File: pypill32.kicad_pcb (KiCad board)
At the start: 2 copper layers, 52.1 x 27.9 mm, 45 parts, among them J1 HeaderR, J2 HeaderL, J3 USB_PINS, J4 SWD_HEADER, SW1 RST_BTN, SW2 BOOT_BTN, U1 SRV05-4, U2 PY32F030F18P6, U3 CH340N, U4 AMS1117-3.3, Y1 32.768 kHz

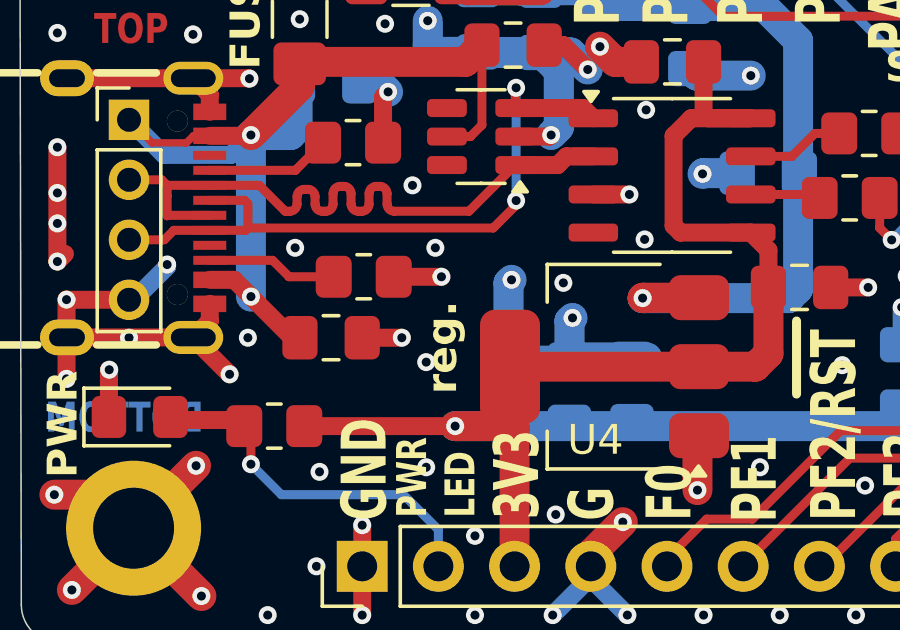
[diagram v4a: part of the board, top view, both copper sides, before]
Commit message: added pad for RTS pin
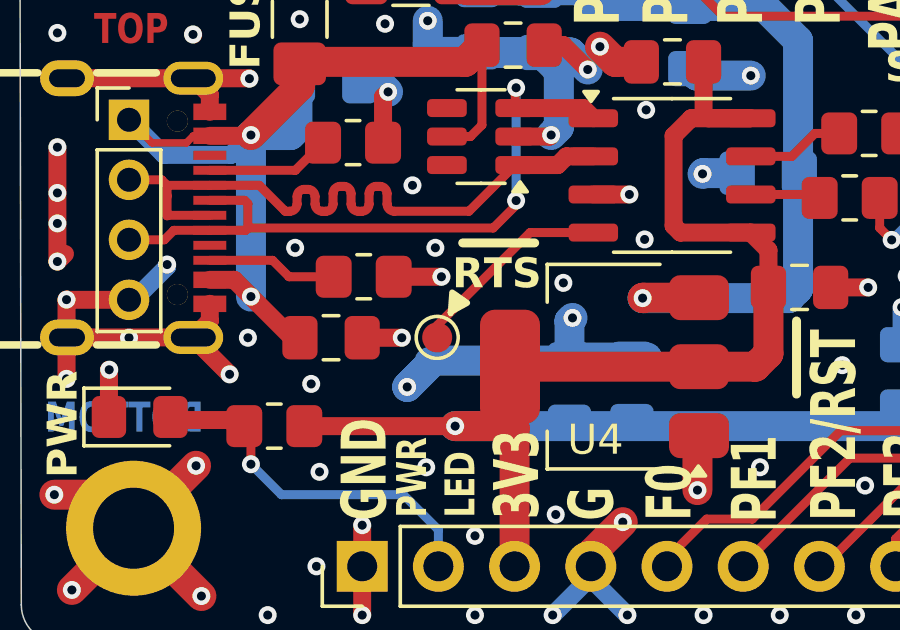
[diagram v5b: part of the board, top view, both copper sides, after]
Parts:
- added TP2: RTS_pad, TestPoint:TestPoint_Pad_D1.0mm, F.Cu at (104.1, 80.0)
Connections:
- U3 pad 4: unconnected-(U3-~{RTS}-Pad4) -> Net-(U3-~{RTS})
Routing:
- net Net-(U3-~{RTS}): track 0.00 -> 6.89 mm
- net GND: track 108.4 -> 110.6 mm
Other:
- board text added: "RTS"
- board text removed: "reg."
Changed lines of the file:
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@@
 	(net 2 "Net-(U3-RXD)")
 	(net 3 "GND")
-	(net 4 "unconnected-(U3-~{RTS}-Pad4)")
+	(net 4 "Net-(U3-~{RTS})")
 	(net 5 "+5V")
 	(net 6 "Net-(U3-TXD)")
@@
 			(layers "F.Cu" "F.Paste" "F.Mask")
 			(roundrect_rratio 0.25)
-			(net 4 "unconnected-(U3-~{RTS}-Pad4)")
+			(net 4 "Net-(U3-~{RTS})")
 			(pinfunction "~{RTS}")
 			(pintype "output")
@@
 		)
 	)
+	(footprint "TestPoint:TestPoint_Pad_D1.0mm"
+		(layer "F.Cu")
+		(at 104.1 80)
+		(descr "SMD pad as test Point, diameter 1.0mm")
+		(tags "test point SMD pad")
+		(property "Reference" "TP2"
+			(at 0 -1.448 0)
+			(layer "F.SilkS")
+			(hide yes)
+			(effects
+				(font
+					(size 1 1)
+					(thickness 0.15)
+				)
+			)
+		)
+		(property "Value" "RTS_pad"
+			(at 0 1.55 0)
+			(layer "F.Fab")
+			(effects
+				(font
+					(size 1 1)
+					(thickness 0.15)
+				)
+			)
+		)
+		(property "Footprint" "TestPoint:TestPoint_Pad_D1.0mm"
+			(at 0 0 0)
+			(unlocked yes)
+			(layer "F.Fab")
+			(hide yes)
+			(effects
+				(font
+					(size 1.27 1.27)
+					(thickness 0.15)
+				)
+			)
+		)
+		(property "Datasheet" ""
+			(at 0 0 0)
+			(unlocked yes)
+			(layer "F.Fab")
+			(hide yes)
+			(effects
+				(font
+					(size 1.27 1.27)
+					(thickness 0.15)
+				)
+			)
+		)
+		(property "Description" "test point"
+			(at 0 0 0)
+			(unlocked yes)
+			(layer "F.Fab")
+			(hide yes)
+			(effects
+				(font
+					(size 1.27 1.27)
+					(thickness 0.15)
+				)
+			)
+		)
+		(property ki_fp_filters "Pin* Test*")
+		(sheetname "Root")
+		(sheetfile "pypill32.kicad_sch")
+		(attr exclude_from_pos_files)
+		(fp_circle
+			(center 0 0)
+			(end 0 0.7)
+			(stroke
+				(width 0.12)
+				(type solid)
+			)
+			(fill none)
+			(layer "F.SilkS")
+		)
+		(fp_circle
+			(center 0 0)
+			(end 1 0)
+			(stroke
+				(width 0.05)
+				(type solid)
+			)
+			(fill none)
+			(layer "F.CrtYd")
+		)
+		(fp_text user "${REFERENCE}"
+			(at 0 -1.45 0)
+			(layer "F.Fab")
+			(effects
+				(font
+					(size 1 1)
+					(thickness 0.15)
+				)
+			)
+		)
+		(pad "1" smd circle
+			(at 0 0)
+			(size 1 1)
+			(layers "F.Cu" "F.Mask")
+			(net 4 "Net-(U3-~{RTS})")
+			(pinfunction "1")
+			(pintype "passive")
+		)
+	)
 	(footprint "Connector_PinHeader_2.54mm:PinHeader_1x12_P2.54mm_Vertical"
 		(layer "F.Cu")
@@
 		(tags "resistor handsolder")
 		(property "Reference" "R6"
-			(at 2.5654 -0.0762 360)
+			(at 2.5654 -0.0762 0)
 			(layer "F.SilkS")
 			(hide yes)
@@
 		)
 		(property "Value" "0R"
-			(at 0 1.65 360)
+			(at 0 1.65 0)
 			(layer "F.Fab")
 			(effects
@@
 		)
 		(property "Footprint" "Resistor_SMD:R_0805_2012Metric_Pad1.20x1.40mm_HandSolder"
-			(at 0 0 360)
+			(at 0 0 0)
 			(layer "F.Fab")
 			(hide yes)
@@
 		)
 		(property "Datasheet" ""
-			(at 0 0 360)
+			(at 0 0 0)
 			(layer "F.Fab")
 			(hide yes)
@@
 		)
 		(property "Description" ""
-			(at 0 0 360)
+			(at 0 0 0)
 			(layer "F.Fab")
 			(hide yes)
@@
 		)
 		(fp_text user "${REFERENCE}"
-			(at 0 0 360)
+			(at 0 0 0)
 			(layer "F.Fab")
 			(effects
@@
 	)
 	(gr_line
+		(start 104.95 76.85)
+		(end 107.35 76.85)
+		(stroke
+			(width 0.3)
+			(type default)
+		)
+		(layer "F.SilkS")
+	)
+	(gr_poly
+		(pts
+			(xy 104.55 79.2) (xy 104.6 78.5) (xy 105.1 78.85) (xy 104.55 79.15)
+		)
+		(stroke
+			(width 0.2)
+			(type solid)
+		)
+		(fill solid)
+		(layer "F.SilkS")
+	)
+	(gr_line
 		(start 135.128 72.136)
 		(end 137.5664 72.136)
@@
 		)
 	)
+	(gr_text "RTS"
+		(at 104.6 78.45 0)
+		(layer "F.SilkS")
+		(effects
+			(font
+				(size 1 1)
+				(thickness 0.25)
+				(bold yes)
+			)
+			(justify left bottom)
+		)
+	)
 	(gr_text "PA2"
 		(at 123.0376 86.0552 90)
@@
 		)
 	)
-	(gr_text "reg."
-		(at 104.8512 81.8896 90)
-		(layer "F.SilkS")
-		(effects
-			(font
-				(size 1 1)
-				(thickness 0.25)
-				(bold yes)
-			)
-			(justify left bottom)
-		)
-	)
 	(gr_text "1"
 		(at 121.158 80.8228 0)
@@
 	)
 	(via
-		(at 103.7336 80.8228)
+		(at 103.1 81.65)
 		(size 0.6)
 		(drill 0.3)
@@
 	)
 	(via
+		(at 99.9 81.55)
+		(size 0.6)
+		(drill 0.3)
+		(layers "F.Cu" "B.Cu")
+		(free yes)
+		(net 3)
+	)
+	(via
 		(at 140.0556 83.6676)
 		(size 0.6)
@@
 	)
 	(via
-		(at 106.5784 78.0796)
-		(size 0.6)
-		(drill 0.3)
-		(layers "F.Cu" "B.Cu")
-		(free yes)
-		(net 3)
-	)
-	(via
 		(at 118.11 63.1952)
 		(size 0.6)
@@
 	(segment
 		(start 106.4768 80.772)
-		(end 106.4768 78.1812)
-		(width 1)
-		(layer "B.Cu")
-		(net 3)
-	)
-	(segment
-		(start 106.4768 80.772)
 		(end 108.4873 80.772)
 		(width 1)
@@
 	)
 	(segment
+		(start 103.978 80.772)
+		(end 106.4768 80.772)
+		(width 1)
+		(layer "B.Cu")
+		(net 3)
+	)
+	(segment
 		(start 105.4608 70.4811)
 		(end 104.0091 70.4811)
@@
 	)
 	(segment
+		(start 103.8352 80.9148)
+		(end 103.8352 80.8228)
+		(width 1)
+		(layer "B.Cu")
+		(net 3)
+	)
+	(segment
 		(start 111.0996 80.6704)
 		(end 108.5889 80.6704)
@@
 	)
 	(segment
-		(start 112.7545 71.2724)
-		(end 112.522 71.0399)
+		(start 103.1 81.65)
+		(end 103.978 80.772)
 		(width 1)
 		(layer "B.Cu")
@@
 	)
 	(segment
-		(start 106.4768 78.1812)
-		(end 106.5784 78.0796)
+		(start 112.7545 71.2724)
+		(end 112.522 71.0399)
 		(width 1)
 		(layer "B.Cu")
@@
 	)
 	(segment
+		(start 103.1 81.65)
+		(end 103.8352 80.9148)
+		(width 1)
+		(layer "B.Cu")
+		(net 3)
+	)
+	(segment
 		(start 109.22 87.63)
 		(end 109.22 87.9856)
@@
 	)
 	(segment
+		(start 104.1 79.6)
+		(end 107.1952 76.5048)
+		(width 0.3)
+		(layer "F.Cu")
+		(net 4)
+	)
+	(segment
+		(start 107.1952 76.5048)
+		(end 109.304 76.5048)
+		(width 0.3)
+		(layer "F.Cu")
+		(net 4)
+	)
+	(segment
+		(start 104.1 80)
+		(end 104.1 79.6)
+		(width 0.3)
+		(layer "F.Cu")
+		(net 4)
+	)
+	(segment

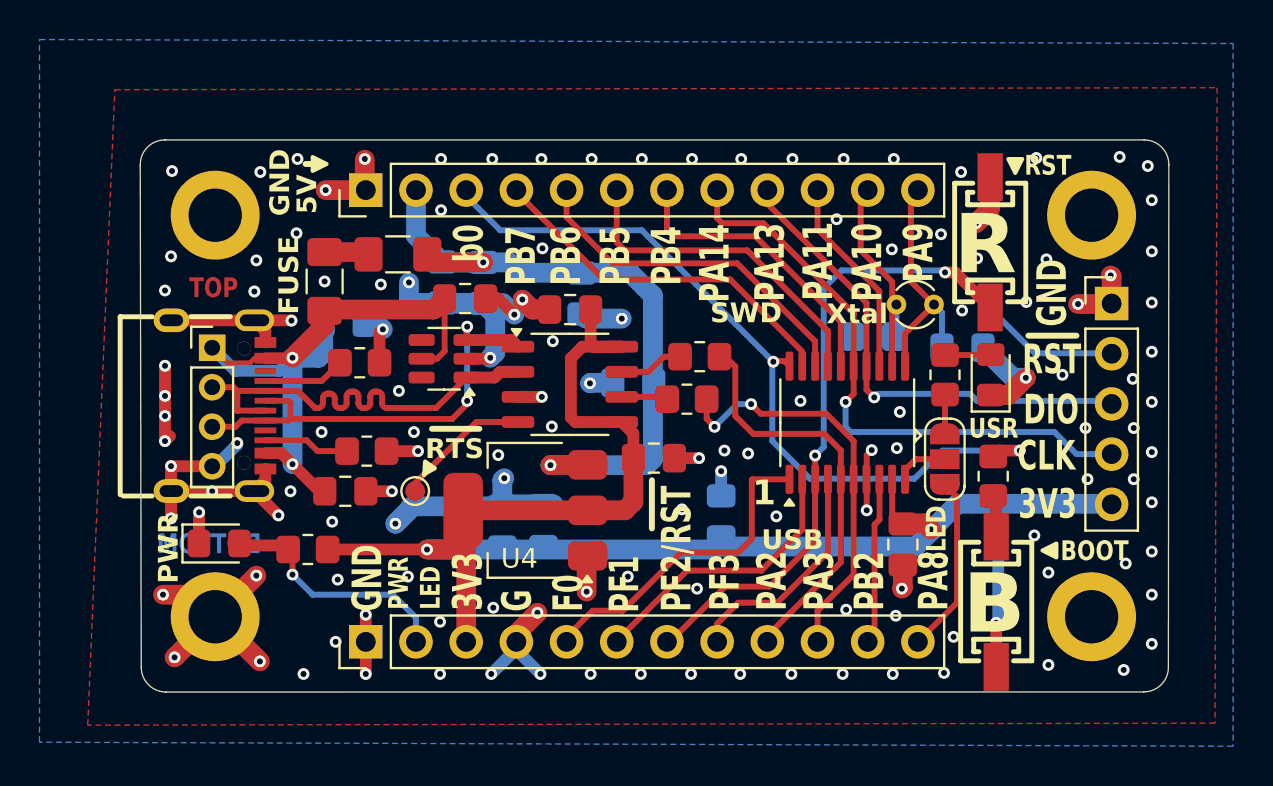
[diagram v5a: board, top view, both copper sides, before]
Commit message: added HF crystal
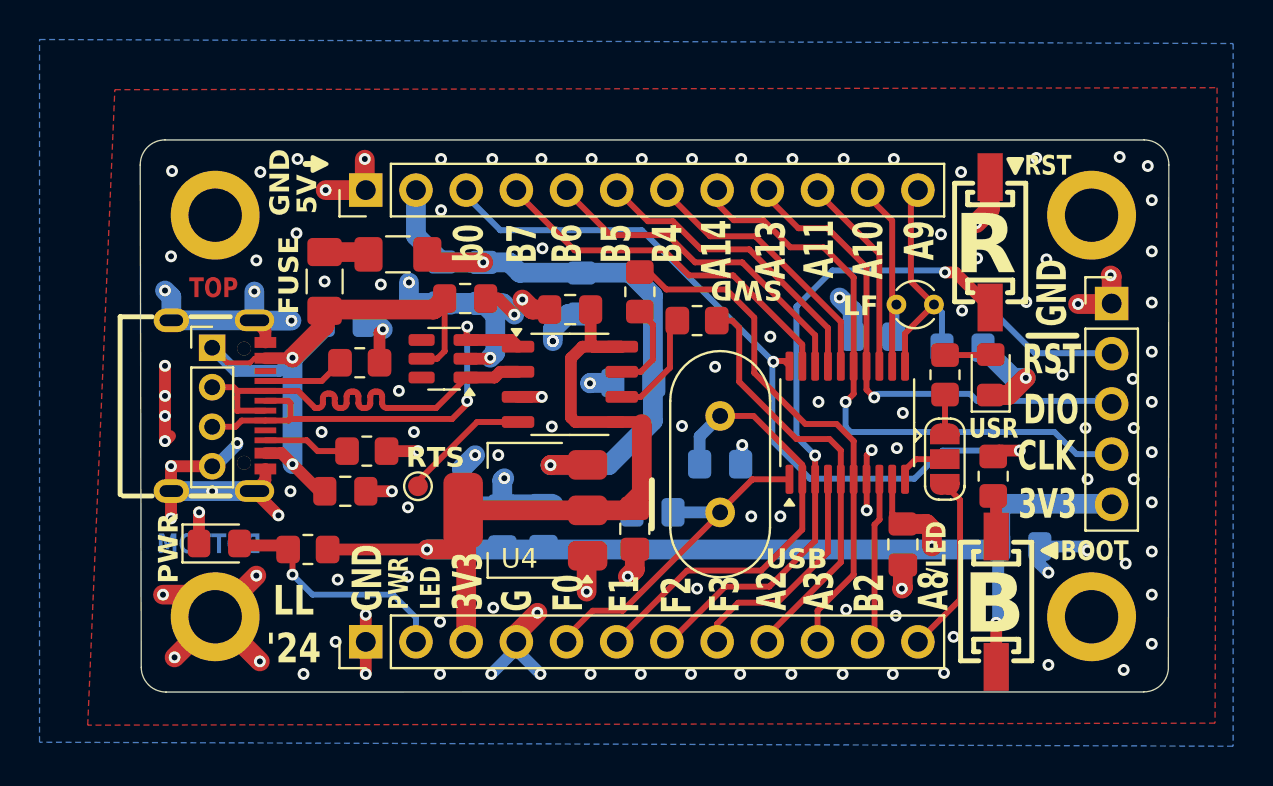
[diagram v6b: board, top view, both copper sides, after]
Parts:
- removed TP2: RTS_pad, TestPoint:TestPoint_Pad_D1.0mm
- added C17: 12p, Capacitor_SMD:C_0805_2012Metric_Pad1.18x1.45mm_HandSolder, B.Cu at (116.1, 81.1)
- added C18: 12p, Capacitor_SMD:C_0805_2012Metric_Pad1.18x1.45mm_HandSolder, B.Cu at (119.5, 78.6)
- added TP1: RTSn, TestPoint:TestPoint_Pad_D1.0mm, F.Cu at (104.2, 79.8)
- added Y2: 12M, Crystal:Crystal_HC49-4H_Vertical, F.Cu at (119.5, 76.2)
- moved C12 15.2 mm to (134.7, 82.8), turned to 0 degrees
- moved R5 4.47 mm to (115.5, 69.9), turned to 90 degrees
- moved R6 4.01 mm to (118.4, 71.4)
- moved C11 3.71 mm to (115.2, 81.9), turned to 90 degrees
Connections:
- R5 pad 2: PYUTX -> PYURX
- R6 pad 2: PYURX -> PYUTX
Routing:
- net GND: track 110.6 -> 122.7 mm, vias 133 -> 132
- net /PF1: track 14.3 -> 23.1 mm
- net PYURX: track 20.8 -> 26.9 mm, vias 2 -> 0
- net +3V3: track 89.0 -> 85.0 mm
- net Net-(U3-TXD): track 2.34 -> 5.59 mm
- net /PB5: track 17.0 -> 15.5 mm
- net Net-(U3-RXD): track 3.26 -> 4.54 mm
- net +5V: track 34.8 -> 33.7 mm
- net /PB4: track 15.0 -> 13.9 mm
- net NRST: track 42.4 -> 43.4 mm
- net SWDIO: track 25.0 -> 25.9 mm
- net VBUS: track 35.9 -> 35.1 mm
- net /PF0: track 16.6 -> 17.3 mm
- net SWDCLK: track 30.3 -> 30.9 mm
- net /PB6: track 17.8 -> 17.2 mm
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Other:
- board text added: "A10"
- board text added: "A11"
- board text added: "A13"
- board text added: "A13=SWDIO"
- board text added: "A14"
- board text added: "A14=SWCLK"
- board text added: "A2"
- board text added: "A3"
- board text added: "A8"
- board text added: "A9"
- board text added: "B2"
- board text added: "B4"
- board text added: "B5"
- board text added: "B6"
- board text added: "B7"
- board text added: "F1"
- board text added: "F2"
- board text added: "F3"
- board text added: "LF"
- board text added: "MCU: PY32F030 F18P6"
- board text removed: "1"
- board text removed: "8kB/64kB"
- board text removed: "PA10"
- board text removed: "PA11"
- board text removed: "PA13"
- board text removed: "PA13=SWDIO"
- board text removed: "PA14"
- board text removed: "PA14=SWCLK"
- board text removed: "PA2"
- board text removed: "PA3"
- board text removed: "PA8"
- board text removed: "PA9"
- board text removed: "PB2"
- board text removed: "PB4"
- board text removed: "PB5"
- board text removed: "PB6"
- board text removed: "PB7"
- board text removed: "PF0"
- board text removed: "PF1"
- board text removed: "PF2/RST"
- board text removed: "PF3"
- board text removed: "PY32F030F18P6"
- board text removed: "RST/PF2"
- board text removed: "Xtal"

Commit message: texts edit
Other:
- board text added: "XTAL"
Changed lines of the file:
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@@
+		)
+	)
+	(gr_text "XTAL"
+		(at 130.2512 69.9516 0)
+		(layer "B.SilkS")
+		(effects
+			(font
+				(size 1 1)
+				(thickness 0.25)
+				(bold yes)
+			)
+			(justify left bottom mirror)
 		)
 	)
@@
 		)
 	)
+	(gr_text "XTAL"
+		(at 114.3 84.4804 0)
+		(layer "B.SilkS")
+		(effects
+			(font
+				(size 1 1)
+				(thickness 0.25)
+				(bold yes)
+			)
+			(justify left bottom mirror)
+		)
+	)
 	(gr_text "B4"
 		(at 117.7544 65.7352 90)
@@
 	(gr_text "A11"
 		(at 125.4252 69.2404 90)
-		(layer "F.SilkS")
+		(layer "F.SilkS" knockout)
 		(effects
 			(font
@@
 	(gr_text "B7"
 		(at 110.3884 68.4784 90)
-		(layer "F.SilkS")
+		(layer "F.SilkS" knockout)
 		(effects
 			(font
@@
 	(gr_text "B5"
 		(at 115.1636 68.4784 90)
-		(layer "F.SilkS")
+		(layer "F.SilkS" knockout)
 		(effects
 			(font
@@
 	(gr_text "B6"
 		(at 112.6744 68.4784 90)
-		(layer "F.SilkS")
+		(layer "F.SilkS" knockout)
 		(effects
 			(font
@@
 	(gr_text "F3"
 		(at 120.65 86.1568 90)
-		(layer "F.SilkS")
+		(layer "F.SilkS" knockout)
 		(effects
 			(font
@@
 	(gr_text "B2"
 		(at 127.9652 86.1568 90)
-		(layer "F.SilkS")
+		(layer "F.SilkS" knockout)
 		(effects
 			(font
@@
 	(gr_text "B4"
 		(at 117.7544 68.4784 90)
-		(layer "F.SilkS")
-		(effects
-			(font
+		(layer "F.SilkS" knockout)
+		(effects
+			(font
